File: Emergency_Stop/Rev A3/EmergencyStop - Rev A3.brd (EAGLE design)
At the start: 55 x 22 mm, 13 parts, among them J3 NC3FBV2-SW, J4 NC3MAV, J5 22-05-7038-03, J6 22-05-7028-02, T1 EXMACHINA-LOGO-NAME

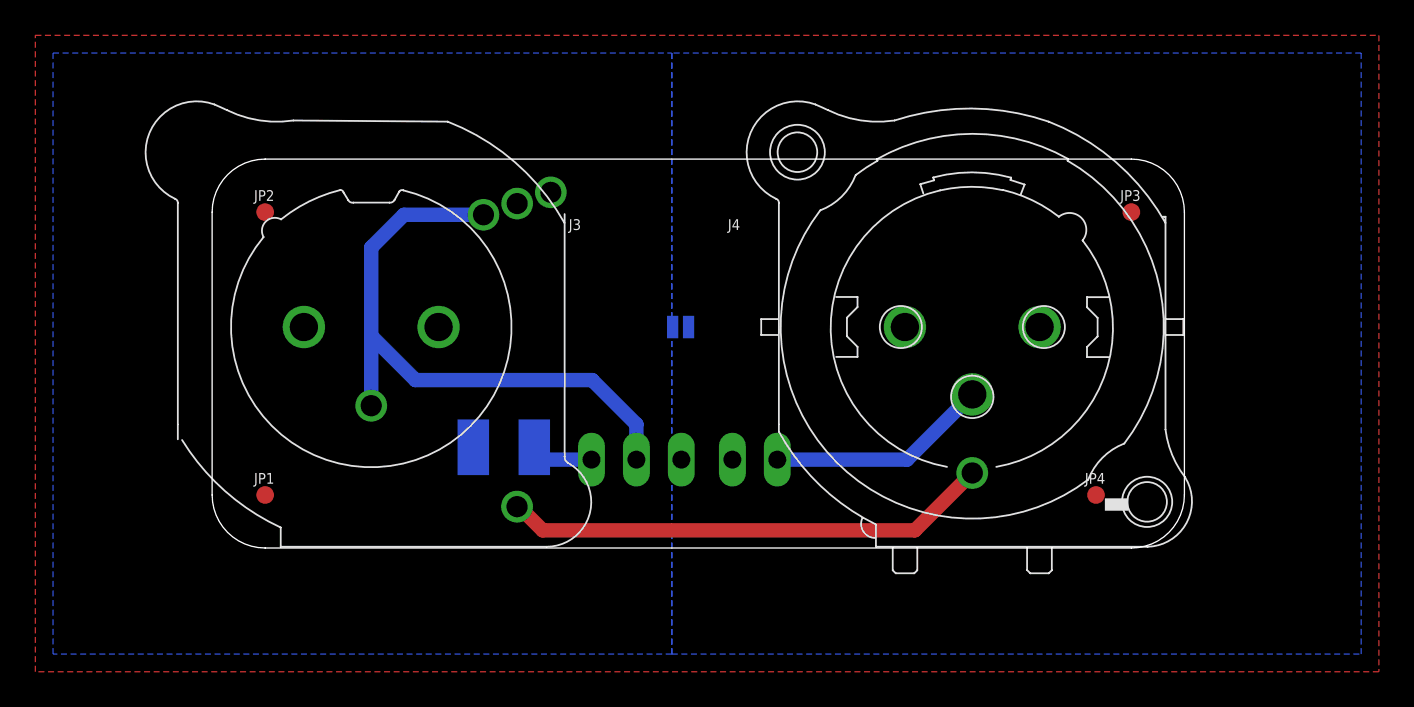
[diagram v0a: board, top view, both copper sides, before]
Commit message: Update EmergencyStop - Rev A3
- Fix layout
- Major redesign in schematics
- Add Lamp output
- Add onboard led
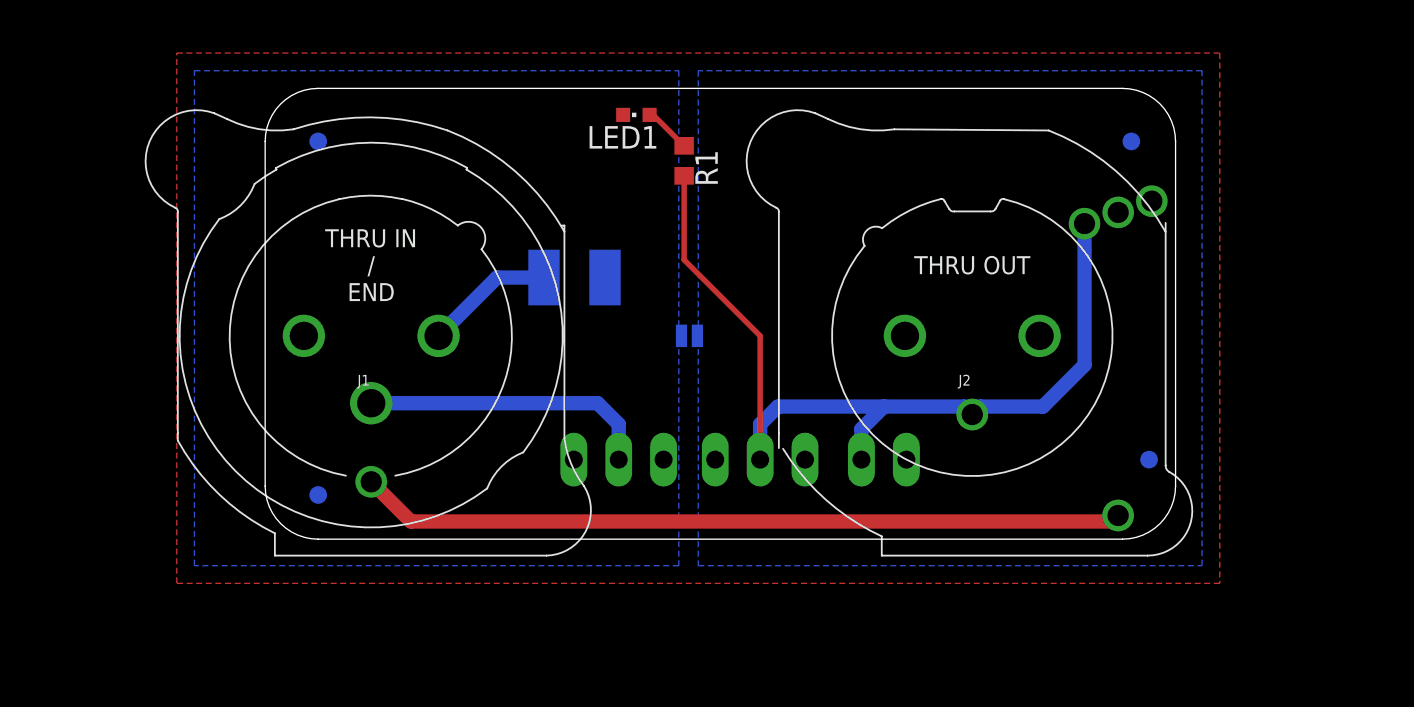
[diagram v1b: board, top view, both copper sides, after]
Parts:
- removed CC1: CC-BY-NC-SA, cc-by-sa:CC-BY-NC-SA
- removed F1: 1812L110/24DR, fuse2:LITTLEFUSE_SMD
- removed J3: NC3FBV2-SW, con-neutrik_ag:NC3FBV2-SW
- removed J4: NC3MAV, con-neutrik_ag:NC3MAV
- removed J5: 22-05-7038-03, con-molex:7395-03
- removed J6: 22-05-7028-02, con-molex:7395-02
- removed JP1, JP2, JP3, JP4: FIDUCIAL1X2, SparkFun:FIDUCIAL-1X2
- removed SJ2: SOLDERJUMPERNO, SparkFun-Passives:SJ_2S-NO
- removed T1: EXMACHINA-LOGO-NAME, exmachina:EXM-LOGO-BASELINE
- added CC100: CC-BY-NC-SA, cc-by-sa:CC-BY-NC-SA
- added F100: 1812L110/24DR, fuse2:LITTLEFUSE_SMD
- added J1: NC3MAV, con-neutrik_ag:NC3MAV
- added J100: 22-05-7028-02, con-molex:7395-02
- added J101, J102: 22-05-7038-03, con-molex:7395-03
- added J2: NC3FBV2-SW, con-neutrik_ag:NC3FBV2-SW
- added JP100, JP101, JP102, JP103: FIDUCIAL1X2, SparkFun:FIDUCIAL-1X2
- added LED1: BLUE, led:CHIPLED_0603
- added R1: 4K7, rcl:R0603
- added SJ100: SOLDERJUMPERNO, SparkFun-Passives:SJ_2S-NO
- added T100: EXMACHINA-LOGO-NAME, exmachina:EXM-LOGO-BASELINE
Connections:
- removed net +24V_IN2: F1.1, J5.1
- new net N$1: F100.1, J1.2
- new net N$2: LED1.A, R1.1
- net +24V_IN: now also F100.2, J102.1, SJ100.2; no longer F1.2, J3.2, J3.C, SJ2.1
- net +24V_OUT: now also J101.1, J2.2, J2.C, SJ100.1; no longer J4.2, J6.1, SJ2.2
- net GND: now also J1.1, J100.2, J101.3, J102.3, J2.1, LED1.C; no longer J3.1, J4.1, J5.3
- net GND_MECA: now also J1.G, J2.G; no longer J3.G, J4.G
- net SIG_IN: now also J1.3, J102.2; no longer J3.3, J3.NC, J5.2
- net SIG_OUT: now also J100.1, J101.2, J2.3, J2.NC, R1.2; no longer J4.3, J6.2
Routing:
- net SIG_OUT: track 12.6 -> 51.5 mm
- net SIG_IN: track 35.1 -> 16.5 mm
- net GND_MECA: track 27.6 -> 43.3 mm
- net N$1: track 0.00 -> 7.33 mm
- net +24V_IN2: track 3.52 -> 0.00 mm
- net N$2: track 0.00 -> 2.67 mm
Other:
- board size 55 x 22 mm -> 51.5 x 25.5 mm
- board text added: "Emergency Stop Rev A3"
- board text added: "THRU IN / END"
- board text added: "THRU OUT"
- board text removed: "Emergency Stop Rev A2"

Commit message: Generate MDP files
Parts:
- moved CC100 5.32 mm to (13.0, 21.5)
- moved JP101 4.03 mm to (49.0, 4.50)
- moved F100 3.04 mm to (17.5, 14.8)
- moved J1 3.04 mm to (6.00, 11.5)
- moved J100 3.04 mm to (35.0, 4.50)
- moved J101 3.04 mm to (28.0, 4.50)
- moved J102 3.04 mm to (20.0, 4.50)
- moved J2 3.04 mm to (40.0, 11.5)
- moved JP100 3.04 mm to (3.00, 2.50)
- moved JP102 3.04 mm to (49.0, 22.5)
- moved JP103 3.04 mm to (3.00, 22.5)
- moved LED1 3.04 mm to (21.0, 24.0)
- moved R1 3.04 mm to (23.7, 21.4)
- moved SJ100 3.04 mm to (24.0, 11.5)
- moved T100 3.04 mm to (42.0, 21.5)
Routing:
- net N$2: track 2.67 -> 3.29 mm
